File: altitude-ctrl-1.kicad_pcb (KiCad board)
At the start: 2 copper layers, 90 x 90 mm, 93 parts, among them J1 Conn_01x02, J10 Conn_01x02, J11 Conn_01x04, J2 Conn_01x02, J3 Conn_01x05, J4 TC2030, J5 Conn_01x04_Pin, J6 Conn_01x02, J7 Conn_01x05, J8 Conn_01x05, J9 Conn_01x02, SW1 SW_Push, SW2 SW_SPST, SW3 SW_Push, SW4 SW_SPST, SW5 SW_Push, U1 HT753-1, U2 ULN2003A, U3 LM73100, U4 LM73100, U5 MAX6675, U6 STM32F103C8Tx, U7 SN65HVD230, Y1 8M

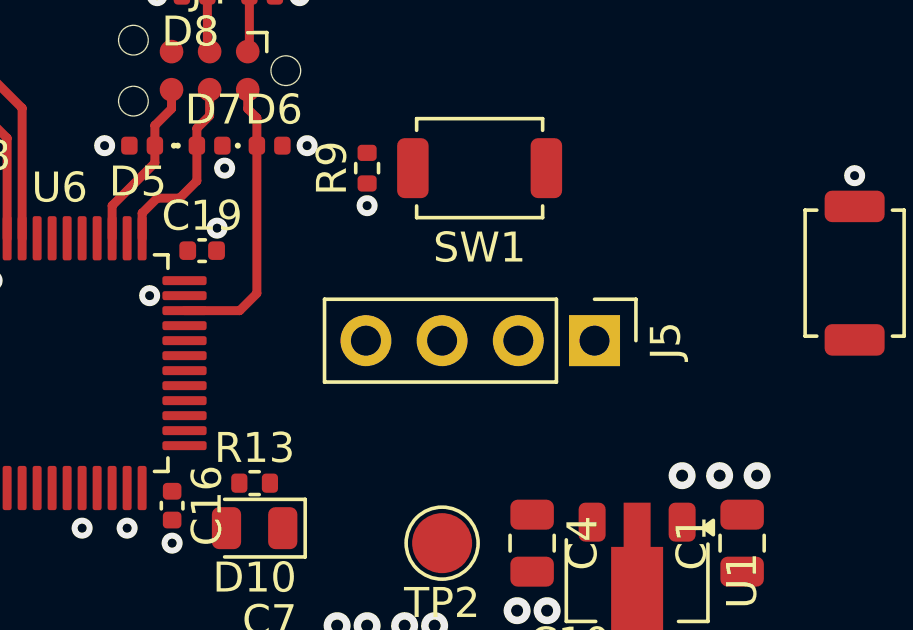
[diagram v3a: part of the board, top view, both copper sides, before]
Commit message: pcb: add uart routing
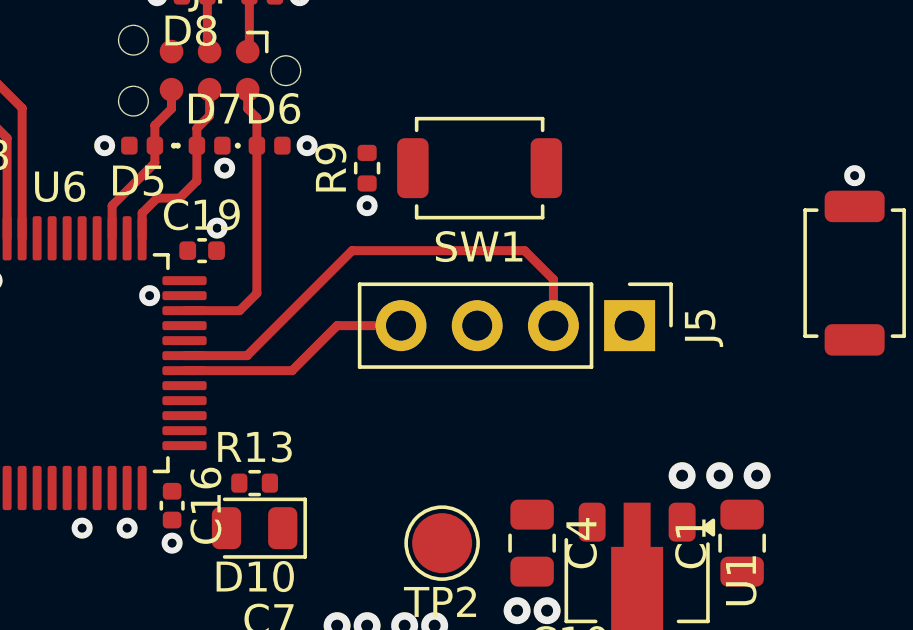
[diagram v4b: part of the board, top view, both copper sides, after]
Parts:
- moved J5 1.27 mm to (183.5, 85.2)
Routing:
- net /U0RXD: track 0.00 -> 15.7 mm
- net /U0TXD: track 0.00 -> 7.84 mm
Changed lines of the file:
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@@
 	(footprint "Connector_PinHeader_2.54mm:PinHeader_1x04_P2.54mm_Vertical"
 		(layer "F.Cu")
-		(at 182.33 85.75 -90)
+		(at 183.5 85.25 -90)
 		(descr "Through hole straight pin header, 1x04, 2.54mm pitch, single row")
 		(tags "Through hole pin header THT 1x04 2.54mm single row")
@@
 	)
 	(segment
+		(start 180.96 83.71)
+		(end 180.96 85.25)
+		(width 0.3)
+		(layer "F.Cu")
+		(net "/U0RXD")
+	)
+	(segment
+		(start 180 82.75)
+		(end 180.96 83.71)
+		(width 0.3)
+		(layer "F.Cu")
+		(net "/U0RXD")
+	)
+	(segment
+		(start 168.6625 86.25)
+		(end 170.75 86.25)
+		(width 0.3)
+		(layer "F.Cu")
+		(net "/U0RXD")
+	)
+	(segment
+		(start 170.75 86.25)
+		(end 174.25 82.75)
+		(width 0.3)
+		(layer "F.Cu")
+		(net "/U0RXD")
+	)
+	(segment
+		(start 174.25 82.75)
+		(end 180 82.75)
+		(width 0.3)
+		(layer "F.Cu")
+		(net "/U0RXD")
+	)
+	(segment
+		(start 173.75 85.25)
+		(end 175.88 85.25)
+		(width 0.3)
+		(layer "F.Cu")
+		(net "/U0TXD")
+	)
+	(segment
+		(start 172.25 86.75)
+		(end 173.75 85.25)
+		(width 0.3)
+		(layer "F.Cu")
+		(net "/U0TXD")
+	)
+	(segment
+		(start 168.6625 86.75)
+		(end 172.25 86.75)
+		(width 0.3)
+		(layer "F.Cu")
+		(net "/U0TXD")
+	)
+	(segment

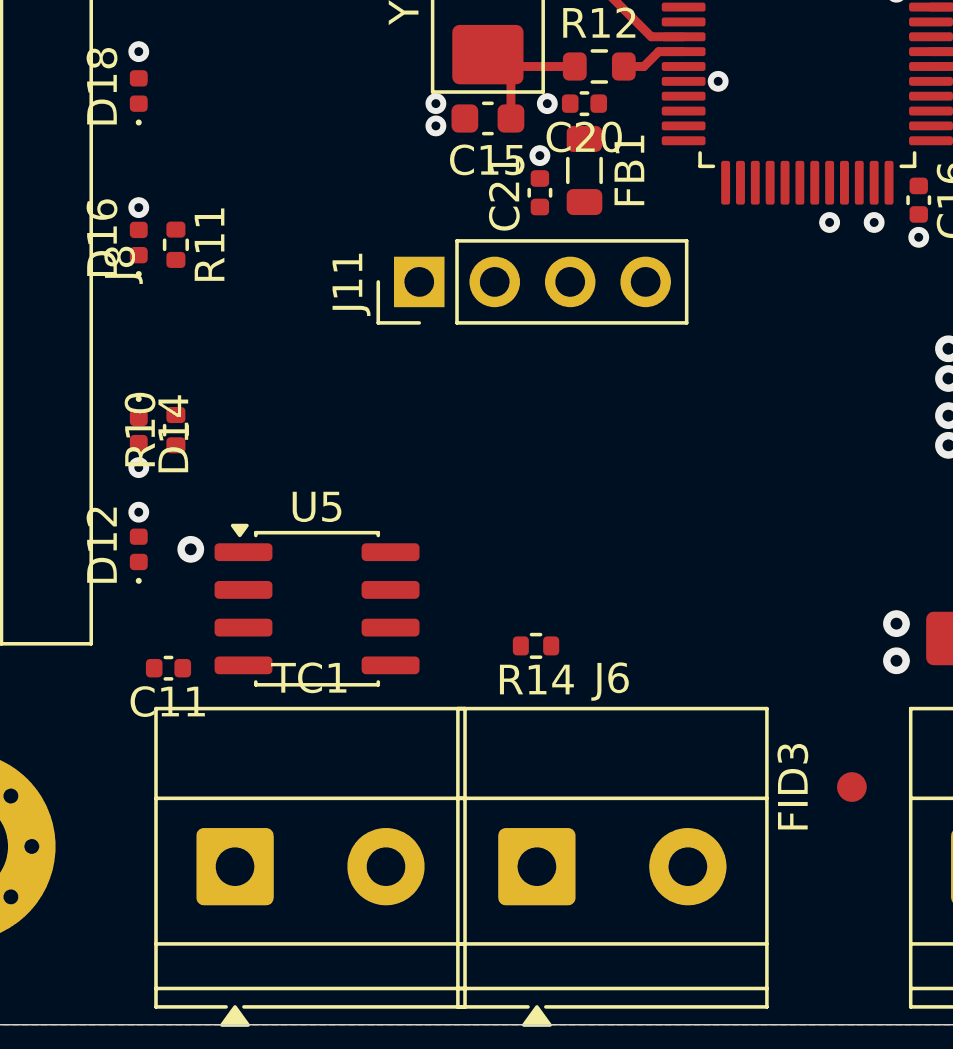
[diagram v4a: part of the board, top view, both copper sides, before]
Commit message: pcb: add spi/thermocouple routing
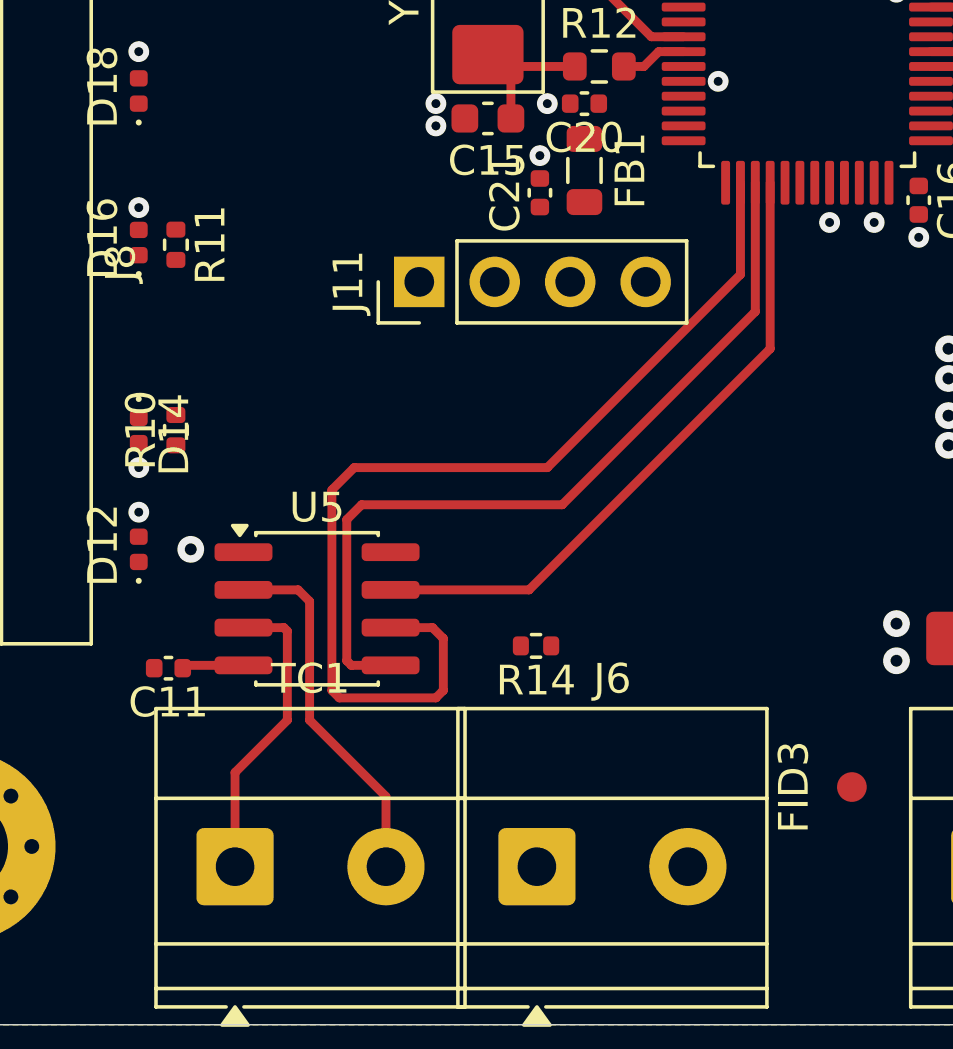
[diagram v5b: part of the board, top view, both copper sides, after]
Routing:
- net /~{CS}: track 0.00 -> 34.2 mm
- net /SCK: track 0.00 -> 27.3 mm
- net /MISO: track 0.00 -> 21.7 mm
- net Net-(TC1--): track 0.00 -> 12.4 mm
- net Net-(TC1-+): track 0.00 -> 10.2 mm
- net +3V3: track 1.89 -> 3.97 mm
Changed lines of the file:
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@@
+	)
+	(segment
+		(start 143.575 106.905)
+		(end 143.48 107)
+		(width 0.3)
+		(layer "F.Cu")
+		(net "+3V3")
 	)
 	(segment
@@
 	)
 	(segment
+		(start 145.525 106.905)
+		(end 143.575 106.905)
+		(width 0.3)
+		(layer "F.Cu")
+		(net "+3V3")
+	)
+	(segment
 		(start 170.77 78.02)
 		(end 171.075 78.325)
@@
 	)
 	(segment
+		(start 152 108)
+		(end 148.75 108)
+		(width 0.3)
+		(layer "F.Cu")
+		(net "/~{CS}")
+	)
+	(segment
+		(start 148.5 107.75)
+		(end 148.5 101)
+		(width 0.3)
+		(layer "F.Cu")
+		(net "/~{CS}")
+	)
+	(segment
+		(start 152.25 107.75)
+		(end 152 108)
+		(width 0.3)
+		(layer "F.Cu")
+		(net "/~{CS}")
+	)
+	(segment
+		(start 152.25 106)
+		(end 152.25 107.75)
+		(width 0.3)
+		(layer "F.Cu")
+		(net "/~{CS}")
+	)
+	(segment
+		(start 148.75 108)
+		(end 148.5 107.75)
+		(width 0.3)
+		(layer "F.Cu")
+		(net "/~{CS}")
+	)
+	(segment
+		(start 162.25 93.750002)
+		(end 162.25 90.6625)
+		(width 0.3)
+		(layer "F.Cu")
+		(net "/~{CS}")
+	)
+	(segment
+		(start 151.885 105.635)
+		(end 152.25 106)
+		(width 0.3)
+		(layer "F.Cu")
+		(net "/~{CS}")
+	)
+	(segment
+		(start 149.25 100.25)
+		(end 155.750002 100.25)
+		(width 0.3)
+		(layer "F.Cu")
+		(net "/~{CS}")
+	)
+	(segment
+		(start 150.475 105.635)
+		(end 151.885 105.635)
+		(width 0.3)
+		(layer "F.Cu")
+		(net "/~{CS}")
+	)
+	(segment
+		(start 155.750002 100.25)
+		(end 162.25 93.750002)
+		(width 0.3)
+		(layer "F.Cu")
+		(net "/~{CS}")
+	)
+	(segment
+		(start 148.5 101)
+		(end 149.25 100.25)
+		(width 0.3)
+		(layer "F.Cu")
+		(net "/~{CS}")
+	)
+	(segment
+		(start 149 106.75)
+		(end 149 102)
+		(width 0.3)
+		(layer "F.Cu")
+		(net "/SCK")
+	)
+	(segment
+		(start 149.155 106.905)
+		(end 149 106.75)
+		(width 0.3)
+		(layer "F.Cu")
+		(net "/SCK")
+	)
+	(segment
+		(start 156.25 101.5)
+		(end 162.75 95)
+		(width 0.3)
+		(layer "F.Cu")
+		(net "/SCK")
+	)
+	(segment
+		(start 162.75 95)
+		(end 162.75 90.6625)
+		(width 0.3)
+		(layer "F.Cu")
+		(net "/SCK")
+	)
+	(segment
+		(start 149.5 101.5)
+		(end 156.25 101.5)
+		(width 0.3)
+		(layer "F.Cu")
+		(net "/SCK")
+	)
+	(segment
+		(start 149 102)
+		(end 149.5 101.5)
+		(width 0.3)
+		(layer "F.Cu")
+		(net "/SCK")
+	)
+	(segment
+		(start 150.475 106.905)
+		(end 149.155 106.905)
+		(width 0.3)
+		(layer "F.Cu")
+		(net "/SCK")
+	)
+	(segment
+		(start 155.135 104.365)
+		(end 150.475 104.365)
+		(width 0.3)
+		(layer "F.Cu")
+		(net "/MISO")
+	)
+	(segment
+		(start 163.25 96.25)
+		(end 155.135 104.365)
+		(width 0.3)
+		(layer "F.Cu")
+		(net "/MISO")
+	)
+	(segment
+		(start 163.25 90.6625)
+		(end 163.25 96.25)
+		(width 0.3)
+		(layer "F.Cu")
+		(net "/MISO")
+	)
+	(segment
 		(start 163.25 78)
 		(end 160.155 74.905)
@@
 		(net "/CANL")
 	)
+	(segment
+		(start 147.75 104.75)
+		(end 147.75 108.75)
+		(width 0.3)
+		(layer "F.Cu")
+		(net "Net-(TC1--)")
+	)
+	(segment
+		(start 150.32 111.32)
+		(end 150.32 113.68)
+		(width 0.3)
+		(layer "F.Cu")
+		(net "Net-(TC1--)")
+	)
+	(segment
+		(start 147.365 104.365)
+		(end 147.75 104.75)
+		(width 0.3)
+		(layer "F.Cu")
+		(net "Net-(TC1--)")
+	)
+	(segment
+		(start 147.75 108.75)
+		(end 150.32 111.32)
+		(width 0.3)
+		(layer "F.Cu")
+		(net "Net-(TC1--)")
+	)
+	(segment
+		(start 145.525 104.365)
+		(end 147.365 104.365)
+		(width 0.3)
+		(layer "F.Cu")
+		(net "Net-(TC1--)")
+	)
+	(segment
+		(start 145.24 110.51)
+		(end 145.24 113.68)
+		(width 0.3)
+		(layer "F.Cu")
+		(net "Net-(TC1-+)")
+	)
+	(segment
+		(start 147 108.75)
+		(end 145.24 110.51)
+		(width 0.3)
+		(layer "F.Cu")
+		(net "Net-(TC1-+)")
+	)
+	(segment
+		(start 147 105.75)
+		(end 147 108.75)
+		(width 0.3)
+		(layer "F.Cu")
+		(net "Net-(TC1-+)")
+	)
+	(segment
+		(start 146.885 105.635)
+		(end 147 105.75)
+		(width 0.3)
+		(layer "F.Cu")
+		(net "Net-(TC1-+)")
+	)
+	(segment
+		(start 145.525 105.635)
+		(end 146.885 105.635)
+		(width 0.3)
+		(layer "F.Cu")
+		(net "Net-(TC1-+)")
+	)
 	(zone

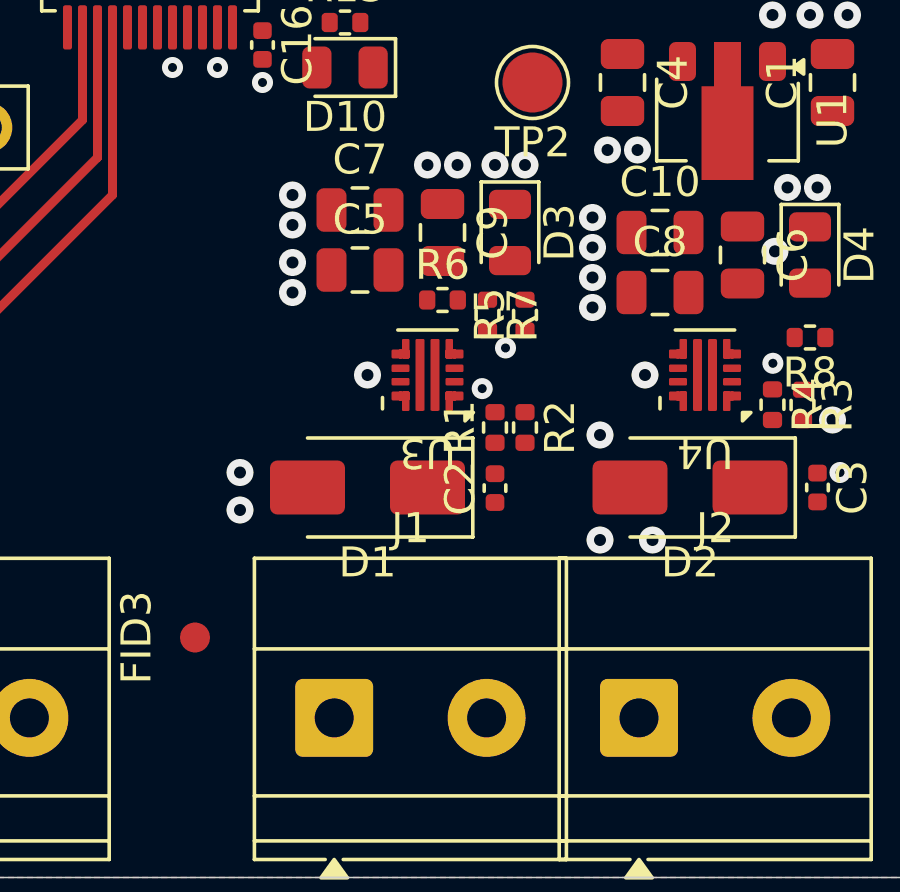
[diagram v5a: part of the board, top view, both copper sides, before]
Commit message: pcb: add +12v efuse routing
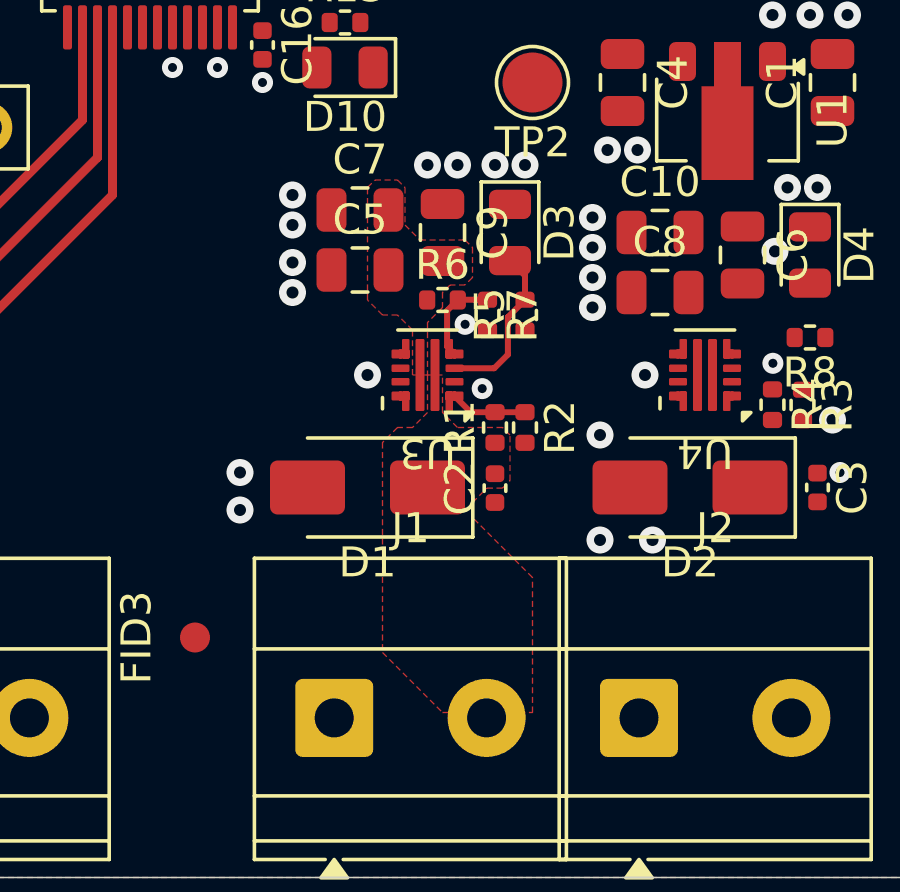
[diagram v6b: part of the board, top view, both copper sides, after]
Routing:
- net Net-(D3-A): track 0.00 -> 5.54 mm
- net Net-(U3-PGTH): track 0.00 -> 3.04 mm
- net Net-(U3-EN/UVLO): track 0.00 -> 2.57 mm
- added copper zone on F.Cu, net +12V
- added copper zone on F.Cu, net +12V_IN
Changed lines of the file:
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@@
 	)
 	(via
-		(at 176.350415 101.349312)
+		(at 175.003878 100.560779)
 		(size 0.7)
 		(drill 0.3)
@@
 	)
 	(segment
+		(start 177 103.49)
+		(end 176 103.49)
+		(width 0.2)
+		(layer "F.Cu")
+		(net "Net-(U3-EN{slash}UVLO)")
+	)
+	(segment
+		(start 174.65 102.95)
+		(end 175.19 103.49)
+		(width 0.2)
+		(layer "F.Cu")
+		(net "Net-(U3-EN{slash}UVLO)")
+	)
+	(segment
+		(start 175.19 103.49)
+		(end 176 103.49)
+		(width 0.2)
+		(layer "F.Cu")
+		(net "Net-(U3-EN{slash}UVLO)")
+	)
+	(segment
+		(start 175.975 102.025)
+		(end 176.43 101.57)
+		(width 0.2)
+		(layer "F.Cu")
+		(net "Net-(D3-A)")
+	)
+	(segment
+		(start 177 99.74)
+		(end 177 98.9375)
+		(width 0.2)
+		(layer "F.Cu")
+		(net "Net-(D3-A)")
+	)
+	(segment
+		(start 174.65 102.025)
+		(end 175.975 102.025)
+		(width 0.2)
+		(layer "F.Cu")
+		(net "Net-(D3-A)")
+	)
+	(segment
+		(start 176.43 101.57)
+		(end 176.43 100.32)
+		(width 0.2)
+		(layer "F.Cu")
+		(net "Net-(D3-A)")
+	)
+	(segment
+		(start 177 99.75)
+		(end 177 99.74)
+		(width 0.2)
+		(layer "F.Cu")
+		(net "Net-(D3-A)")
+	)
+	(segment
+		(start 177 98.9375)
+		(end 176.5 98.4375)
+		(width 0.2)
+		(layer "F.Cu")
+		(net "Net-(D3-A)")
+	)
+	(segment
+		(start 176.43 100.32)
+		(end 177 99.75)
+		(width 0.2)
+		(layer "F.Cu")
+		(net "Net-(D3-A)")
+	)
+	(segment
+		(start 175.75 99.74)
+		(end 174.77 99.74)
+		(width 0.2)
+		(layer "F.Cu")
+		(net "Net-(U3-PGTH)")
+	)
+	(segment
+		(start 174.65 101.55)
+		(end 174.403878 101.303878)
+		(width 0.2)
+		(layer "F.Cu")
+		(net "Net-(U3-PGTH)")
+	)
+	(segment
+		(start 174.77 99.74)
+		(end 174.76 99.75)
+		(width 0.2)
+		(layer "F.Cu")
+		(net "Net-(U3-PGTH)")
+	)
+	(segment
+		(start 174.403878 100.106122)
+		(end 174.76 99.75)
+		(width 0.2)
+		(layer "F.Cu")
+		(net "Net-(U3-PGTH)")
+	)
+	(segment
+		(start 174.403878 101.303878)
+		(end 174.403878 100.106122)
+		(width 0.2)
+		(layer "F.Cu")
+		(net "Net-(U3-PGTH)")
+	)
+	(segment
 		(start 152 108)
 		(end 148.75 108)
@@
 	)
 	(zone
+		(net "+12V")
+		(layer "F.Cu")
+		(hatch edge 0.5)
+		(priority 2)
+		(connect_pads yes
+			(clearance 0.2)
+		)
+		(min_thickness 0.15)
+		(fill yes
+			(thermal_gap 0.5)
+			(thermal_bridge_width 0.5)
+			(island_removal_mode 0)
+		)
+		(polygon
+			(pts
+				(xy 173 97.25) (xy 173.5 97.75) (xy 175 97.75) (xy 175.25 98) (xy 175.25 99) (xy 175 99.25) (xy 174.5 99.25)
+				(xy 174.25 99.5) (xy 174.25 100) (xy 173.75 100.5) (xy 173.75 102.25) (xy 173.25 102.25) (xy 173.25 100.75)
+				(xy 172.75 100.25) (xy 172.25 100.25) (xy 171.75 99.75) (xy 171.75 96) (xy 172 95.75) (xy 172.75 95.75)
+				(xy 173 96)
+			)
+		)
+	)
+	(zone
+		(net "+12V_IN")
+		(layer "F.Cu")
+		(hatch edge 0.5)
+		(priority 1)
+		(connect_pads yes
+			(clearance 0.2)
+		)
+		(min_thickness 0.15)
+		(fill yes
+			(thermal_gap 0.5)
+			(thermal_bridge_width 0.5)
+			(island_removal_mode 0)
+		)
+		(polygon
+			(pts
+				(xy 177.25 113.5) (xy 177.25 109) (xy 175.25 107) (xy 175.25 106.5) (xy 175.73 106.02) (xy 176.25 106.02)
+				(xy 176.5 105.77) (xy 176.5 104.25) (xy 176.25 104) (xy 174.75 104) (xy 174.25 103.5) (xy 174.25 102.25)
+				(xy 173.75 102.25) (xy 173.75 103.5) (xy 173.25 104) (xy 172.75 104) (xy 172.25 104.5) (xy 172.25 111.5)
+				(xy 174.25 113.5)
+			)
+		)
+	)
+	(zone
